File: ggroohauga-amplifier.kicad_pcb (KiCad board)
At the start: 2 copper layers, 95 x 31 mm, 9 parts

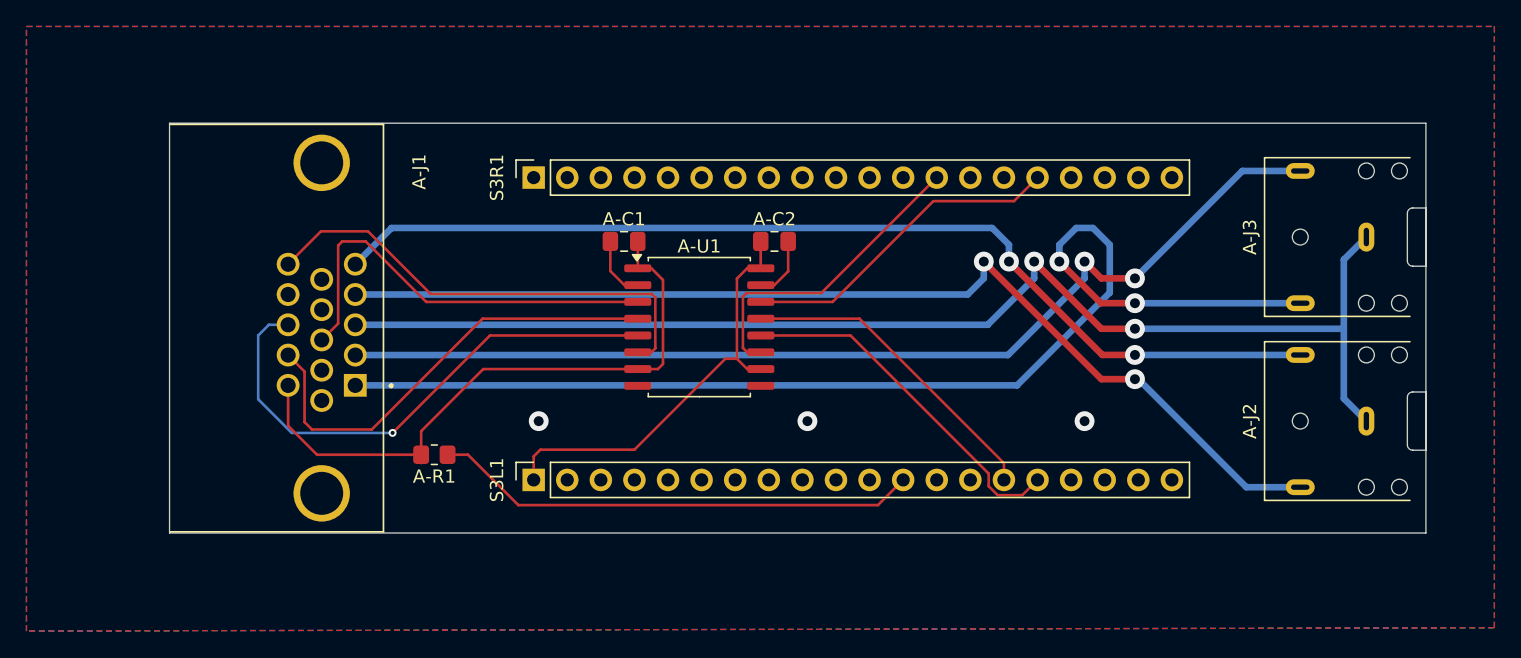
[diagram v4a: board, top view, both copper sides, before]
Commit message: Make all the PCBs a regular size, to 0.5mm
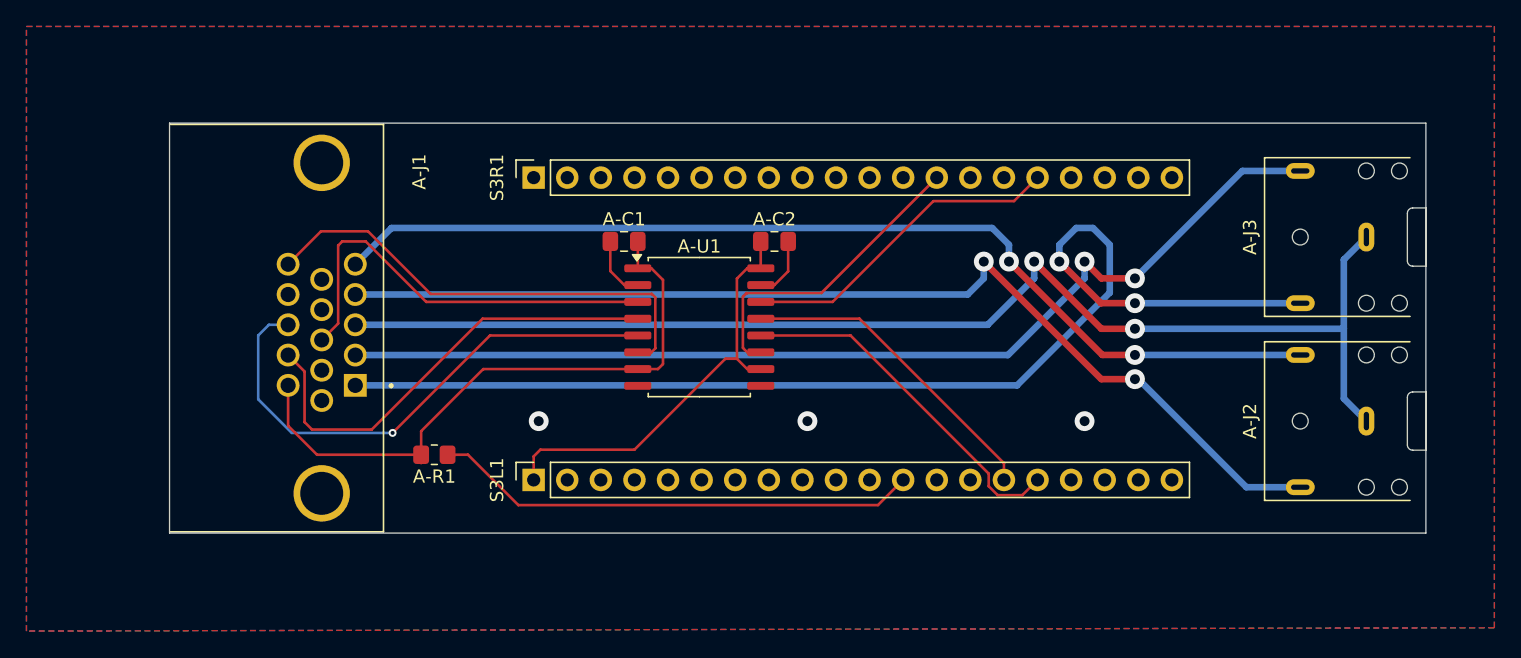
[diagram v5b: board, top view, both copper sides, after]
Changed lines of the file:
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@@
 	)
 	(gr_rect
-		(start 54 50.4952)
-		(end 149 81.4832)
+		(start 54 50.4892)
+		(end 149 81.4892)
 		(stroke
 			(width 0.0254)
@@
 	)
 	(gr_text "JLCJLCJLCJLC"
-		(at 138.176 58.42 90)
+		(at 134.144 58.42 90)
 		(layer "B.SilkS")
 		(effects
